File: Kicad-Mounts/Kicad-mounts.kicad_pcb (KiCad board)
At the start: 2 copper layers, 25 x 35.8 mm, 8 parts, among them P3 CONN_6X2, P6 CONN_3, U2 TPS77033

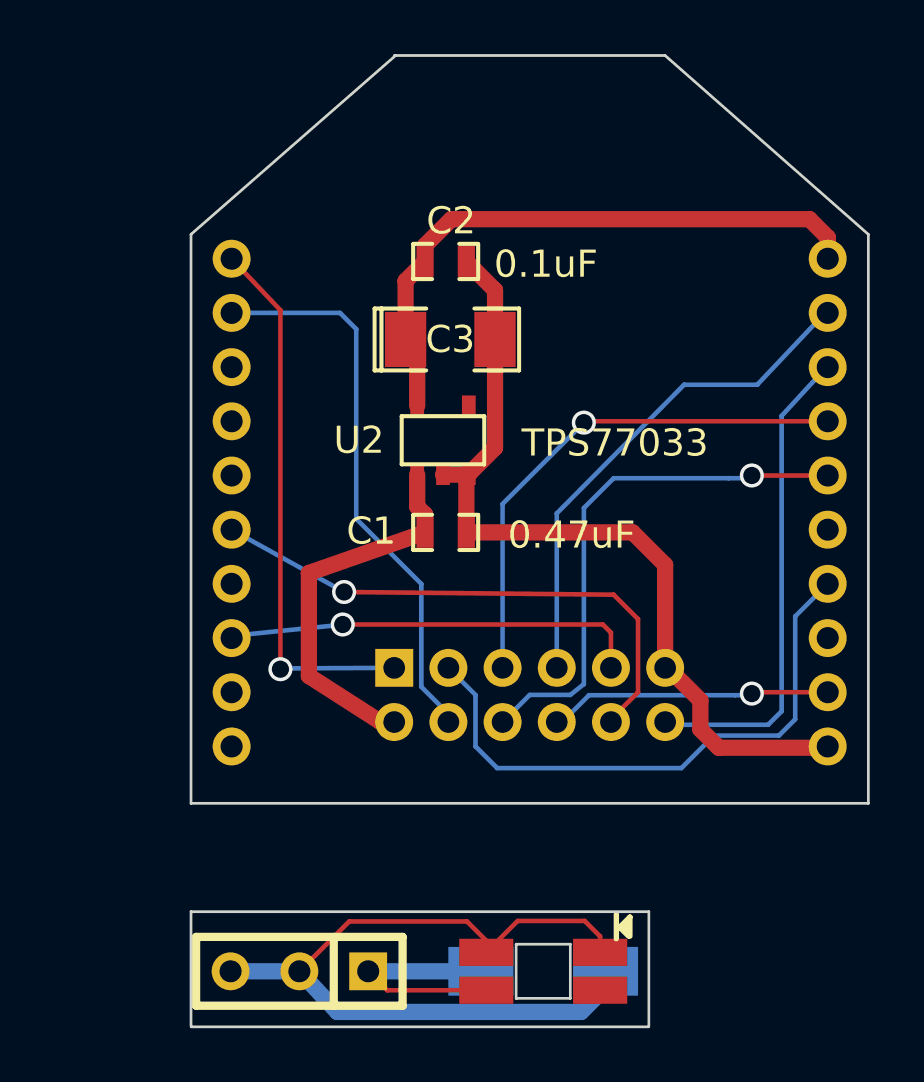
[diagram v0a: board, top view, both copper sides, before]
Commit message: Update Mounts board to force metric drill sizes and join to LED board with a slot
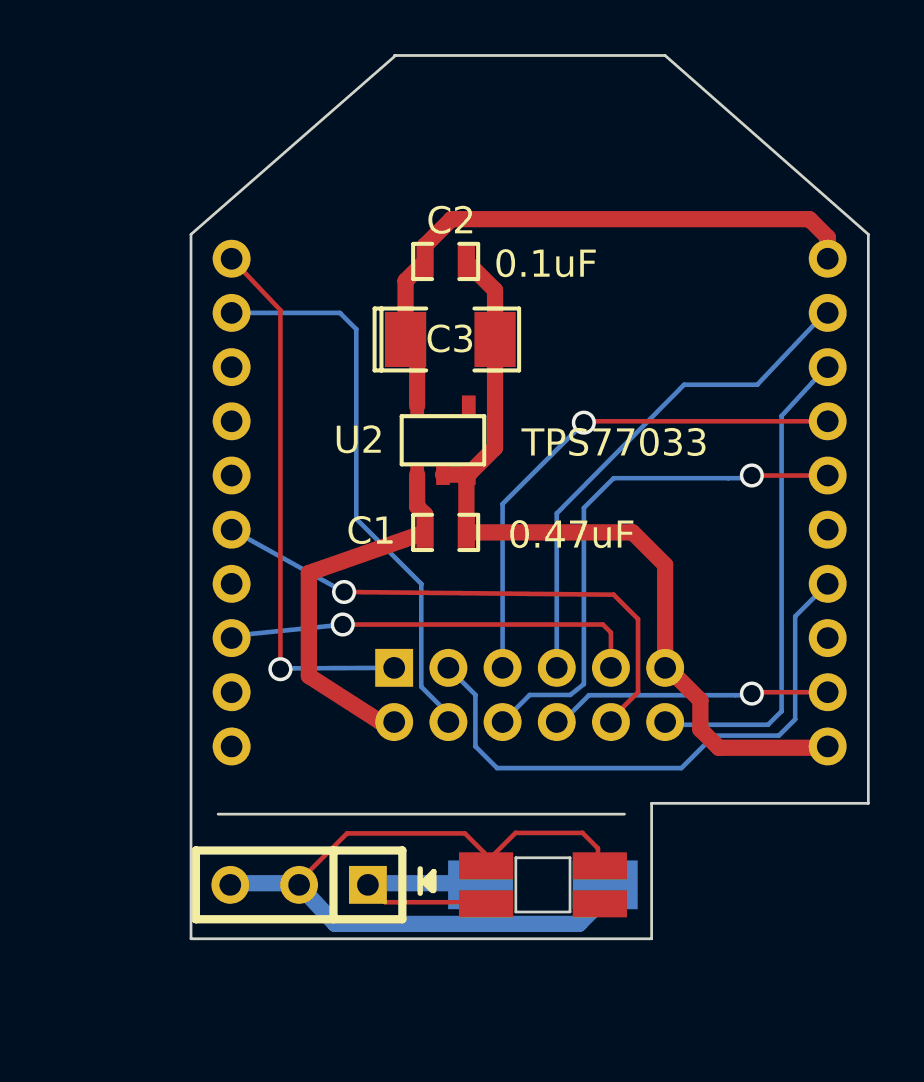
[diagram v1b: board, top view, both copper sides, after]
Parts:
- moved D1 3.19 mm to (181.1, 121.0)
- moved P6 3.19 mm to (172.0, 121.0)
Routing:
- net Net-(D1-Pad2): track 9.23 -> 8.61 mm
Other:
- board size 25 x 35.8 mm -> 25 x 32.6 mm

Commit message: Update of Mounts boards PCBs and generation of gerbers.
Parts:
- added G***: LOGO, Photodiode:Xerofill-Logo, F.Cu at (180.3, 94.2)
- moved D1 22.7 mm to (165.2, 104.8), turned to 90 degrees
- moved P6 9.82 mm to (165.2, 113.9), turned to 270 degrees
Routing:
- net /Sleep_Rq: track 11.0 -> 21.6 mm, vias 1 -> 0
- net /Commissioning: track 20.1 -> 26.6 mm, vias 1 -> 0
- net /Tx: track 18.1 -> 23.9 mm
- net /Reset: track 19.3 -> 23.6 mm, vias 1 -> 0
- net /XBee-Reset: track 20.2 -> 21.3 mm, vias 1 -> 0
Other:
- board size 25 x 32.6 mm -> 30 x 27.6 mm
- board text added: "Rev 2.00"
